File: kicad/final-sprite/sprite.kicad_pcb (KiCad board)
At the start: 4 copper layers, 35 x 44.6 mm, 66 parts, among them J1 M20-7910442R, U1 CC430F513X, U2 LSM9DS1, U3 SPRITETCXO_TCXO_7Z, U4 DRV8837, U5 ADP5092, U6 DRV8837, U7 DRV8837, X1 SPRITEPIN_SPRITE_PIN, X2 SPRITEPIN_SPRITE_PIN

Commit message: Save supercap footprint in sprite library
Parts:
- C10: footprint CAPCP3225X100N -> sprite:CAPCP3225X100N
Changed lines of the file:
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@@
-(kicad_pcb (version 20171130) (host pcbnew 6.0.0-rc1-unknown-3eb3db0~66~ubuntu16.04.1)
+(kicad_pcb (version 20171130) (host pcbnew "(5.1.0-dev-136-geef31e476)")
   (general
     (thickness 0.7874)
@@
     (add_net VCCIO)
   )
-  (module CAPCP3225X100N (layer Bottom)
+  (module sprite:CAPCP3225X100N (layer Bottom)
     (at 153.67 99.441)
     (fp_text reference C10 (at -1.50651 1.50651) (layer B.SilkS)

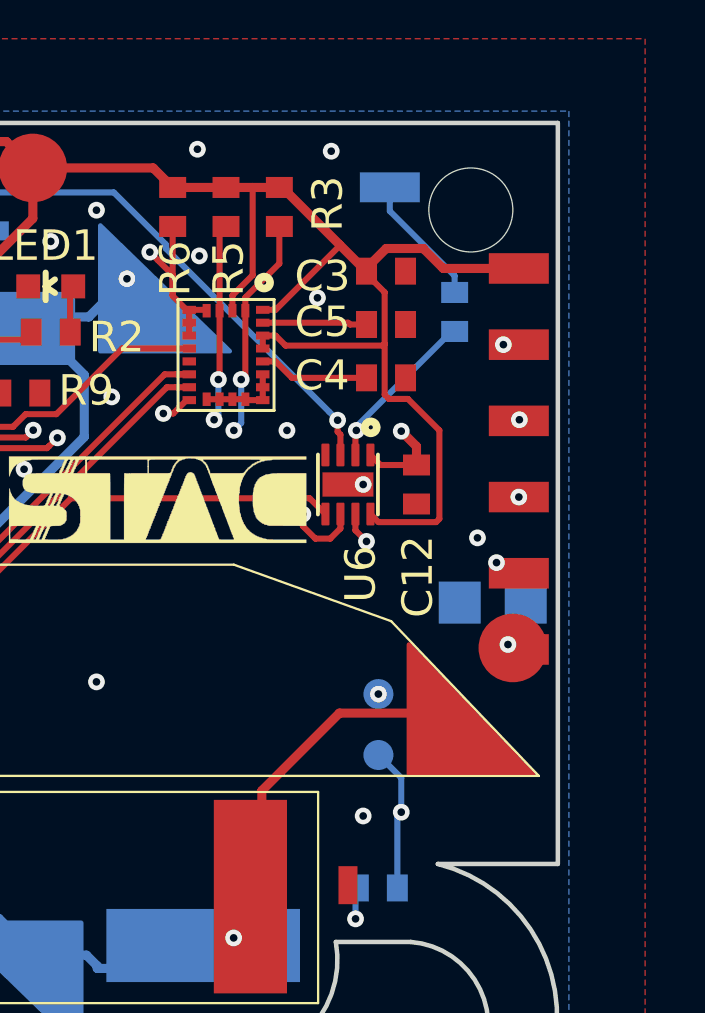
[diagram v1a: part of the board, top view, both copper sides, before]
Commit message: Dump in a few more supercaps
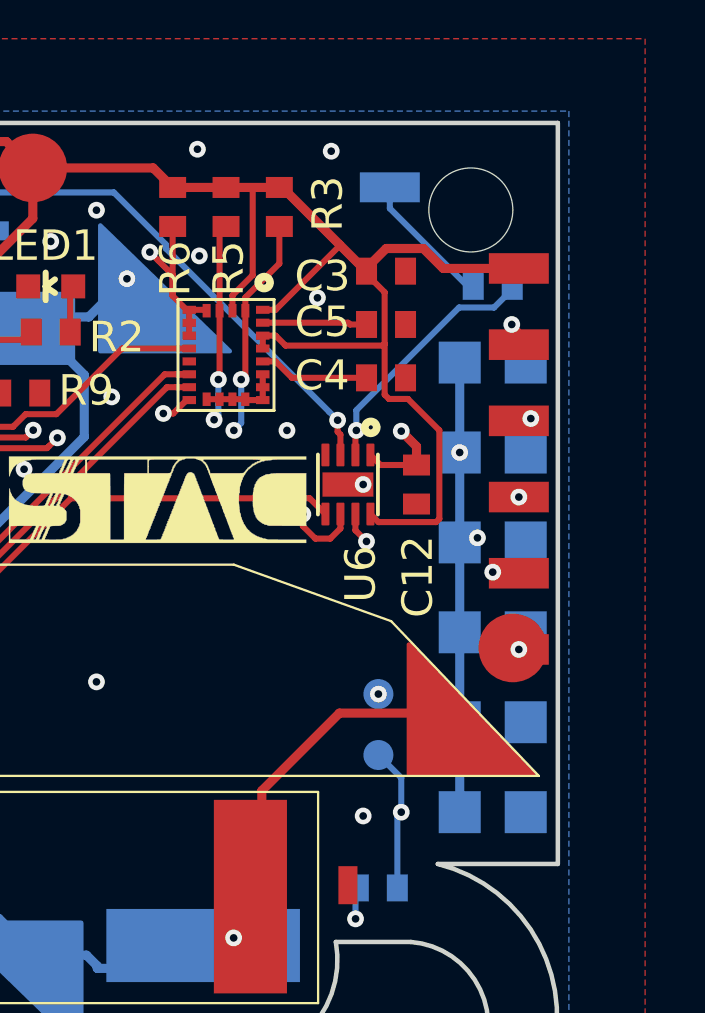
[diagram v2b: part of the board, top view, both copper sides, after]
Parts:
- added C18: CPH3225A, sprite:CAPCP3225X100N, B.Cu at (153.7, 106.4)
- added C19: CPH3225A, sprite:CAPCP3225X100N, B.Cu at (153.7, 103.4)
- added C20: CPH3225A, sprite:CAPCP3225X100N, B.Cu at (153.7, 97.4)
- added C21: CPH3225A, sprite:CAPCP3225X100N, B.Cu at (153.7, 94.4)
- added C22: CPH3225A, sprite:CAPCP3225X100N, B.Cu at (153.7, 91.4)
- moved R12 1.53 mm to (153.7, 88.9), turned to 180 degrees
- moved C10 0.99 mm to (153.7, 100.4)
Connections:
- C10 pad 1: Net-(C10-Pad1) -> /VBAT
- C10 pad 2: Net-(C10-Pad2) -> GND
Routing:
- net /VBAT: track 25.6 -> 39.0 mm, vias 1 -> 3
- net Net-(R12-Pad1): track 5.54 -> 8.59 mm
- net /~RST: track 51.2 -> 52.0 mm
- net /TST: track 54.3 -> 53.8 mm
- net GND: vias 29 -> 28

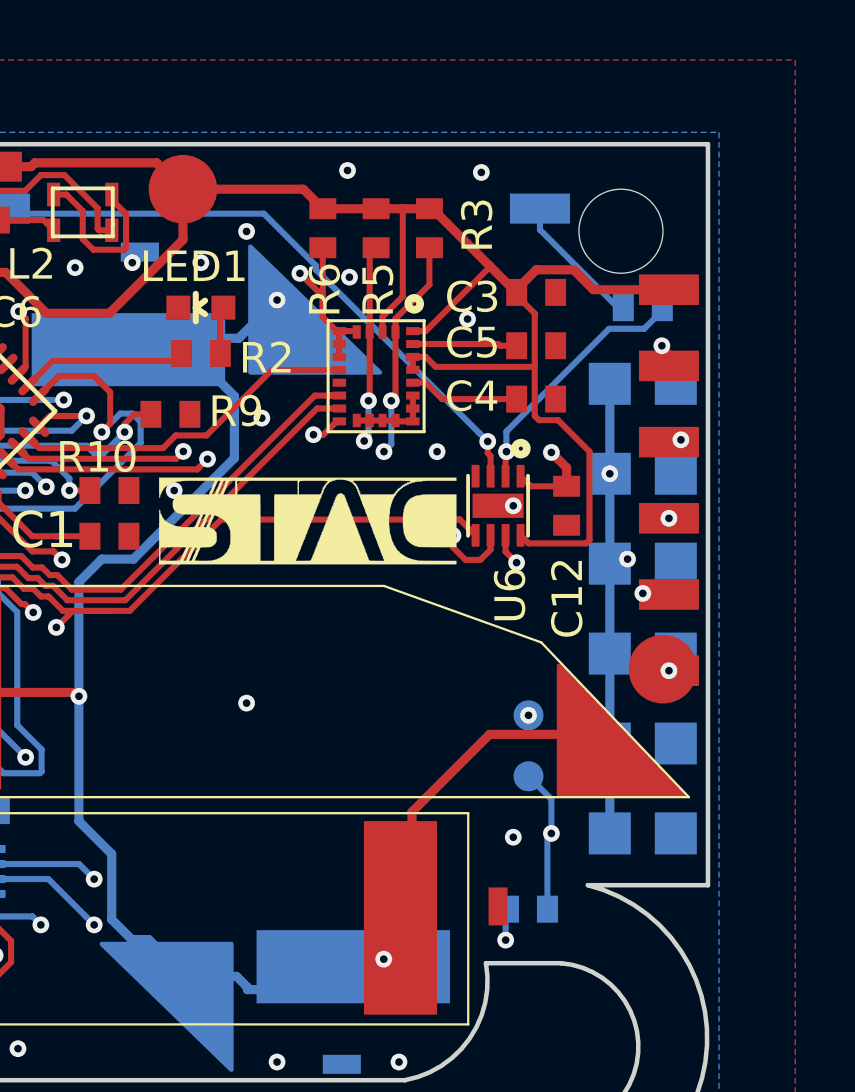
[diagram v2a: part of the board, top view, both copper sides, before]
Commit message: added more caps and moved a couple traces
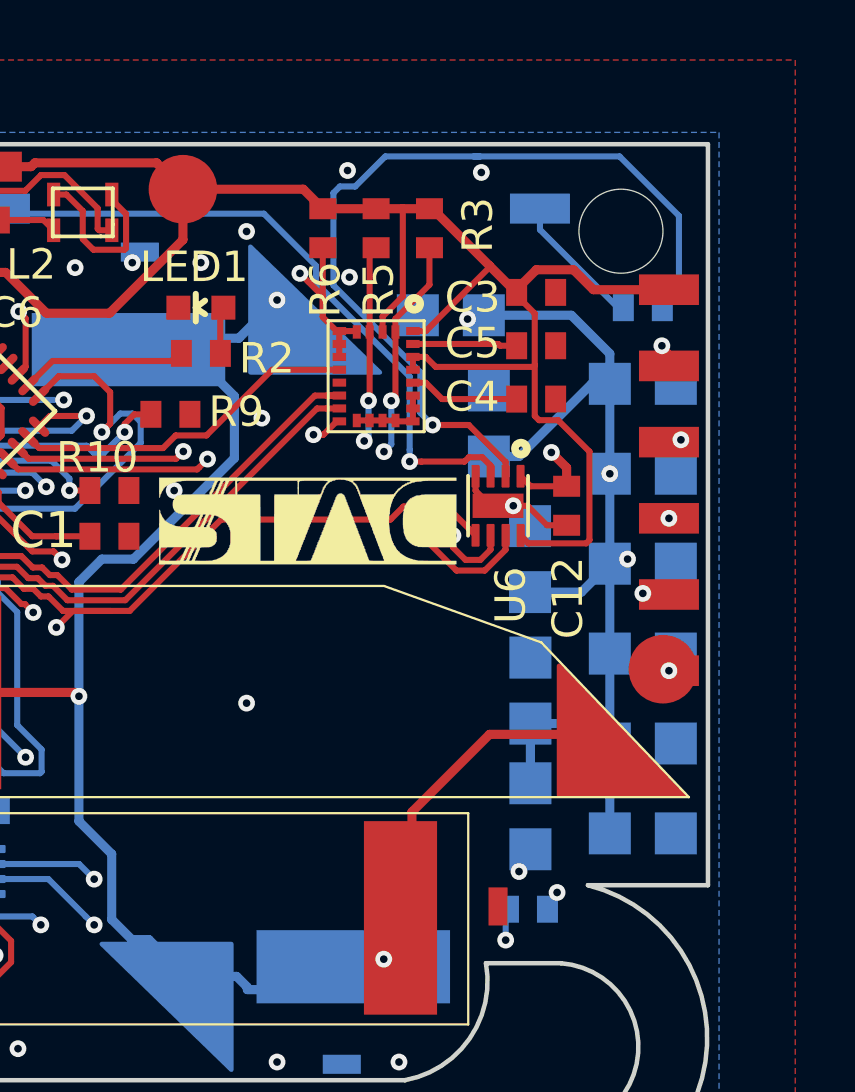
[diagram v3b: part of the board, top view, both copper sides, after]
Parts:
- removed TP1, TP2: Test_Point, TestPoint:TestPoint_Pad_D1.0mm
- added C23: CPH3225A, sprite:CAPCP3225X100N, B.Cu at (149.9, 105.9)
- added C24: CPH3225A, sprite:CAPCP3225X100N, B.Cu at (149.9, 101.7)
- added C25: CPH3225A, sprite:CAPCP3225X100N, B.Cu at (147.3, 89.2)
- added C26: CPH3225A, sprite:CAPCP3225X100N, B.Cu at (149.9, 97.3)
- added C27: CPH3225A, sprite:CAPCP3225X100N, B.Cu at (148.5, 92.8)
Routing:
- net Net-(R12-Pad1): track 8.59 -> 29.0 mm
- net /VBAT: track 39.0 -> 58.2 mm, vias 3 -> 4
- net Net-(R22-Pad1): track 736.5 -> 725.8 mm, vias 4 -> 3
- net GND: track 38.2 -> 42.2 mm, vias 28 -> 26
- net Net-(L4-Pad2): track 20.7 -> 22.3 mm

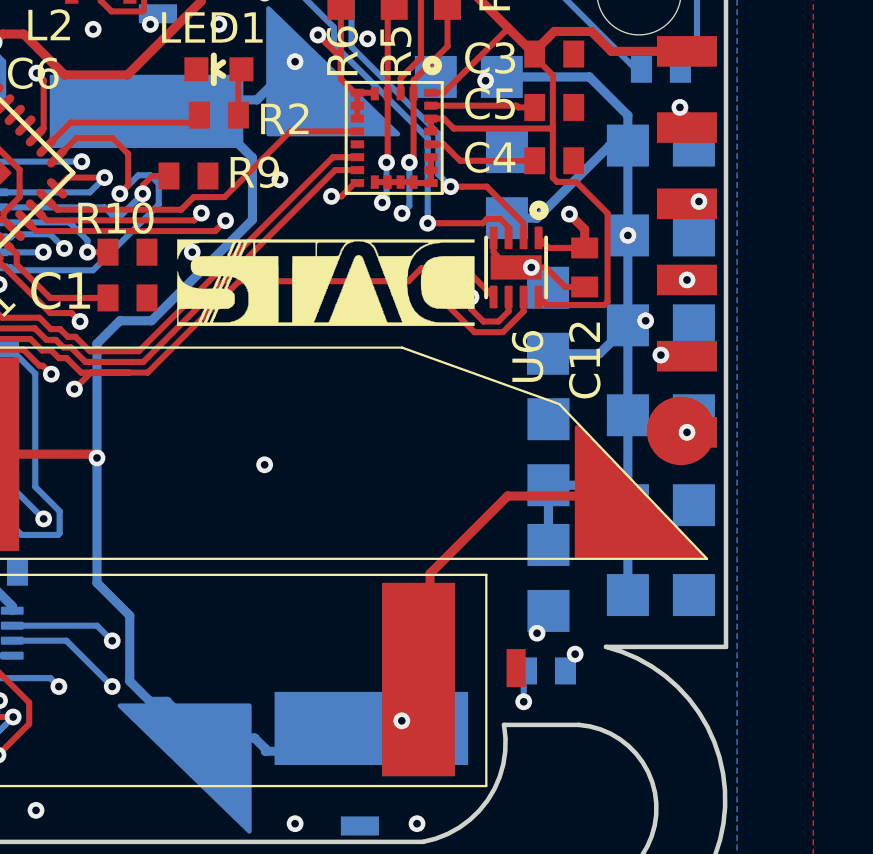
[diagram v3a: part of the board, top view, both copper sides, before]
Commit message: routes fixed, no DRC violations, 11 new caps
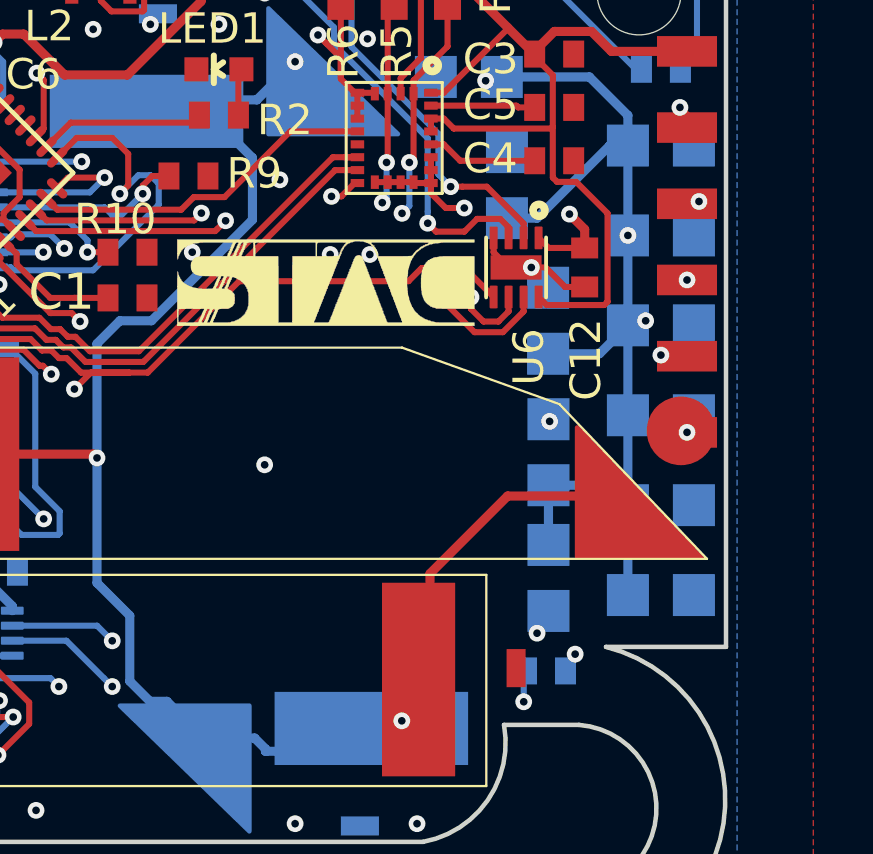
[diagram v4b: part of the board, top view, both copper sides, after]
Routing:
- net GND: track 42.2 -> 43.9 mm, vias 26 -> 30
- net Net-(R22-Pad1): track 725.8 -> 726.5 mm

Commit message: Remove silkscreen logo on back
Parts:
- removed the G*** at (149.6, 96.0)
